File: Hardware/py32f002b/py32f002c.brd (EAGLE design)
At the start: 43.9 x 18.6 mm, 26 parts, among them IC1 PY32F002BF15P6TU, IC2 AP2114HA-3.3TRG1, J1 USB_MINI-B_SMT, Y1 DSC6083CI1A-350K000T

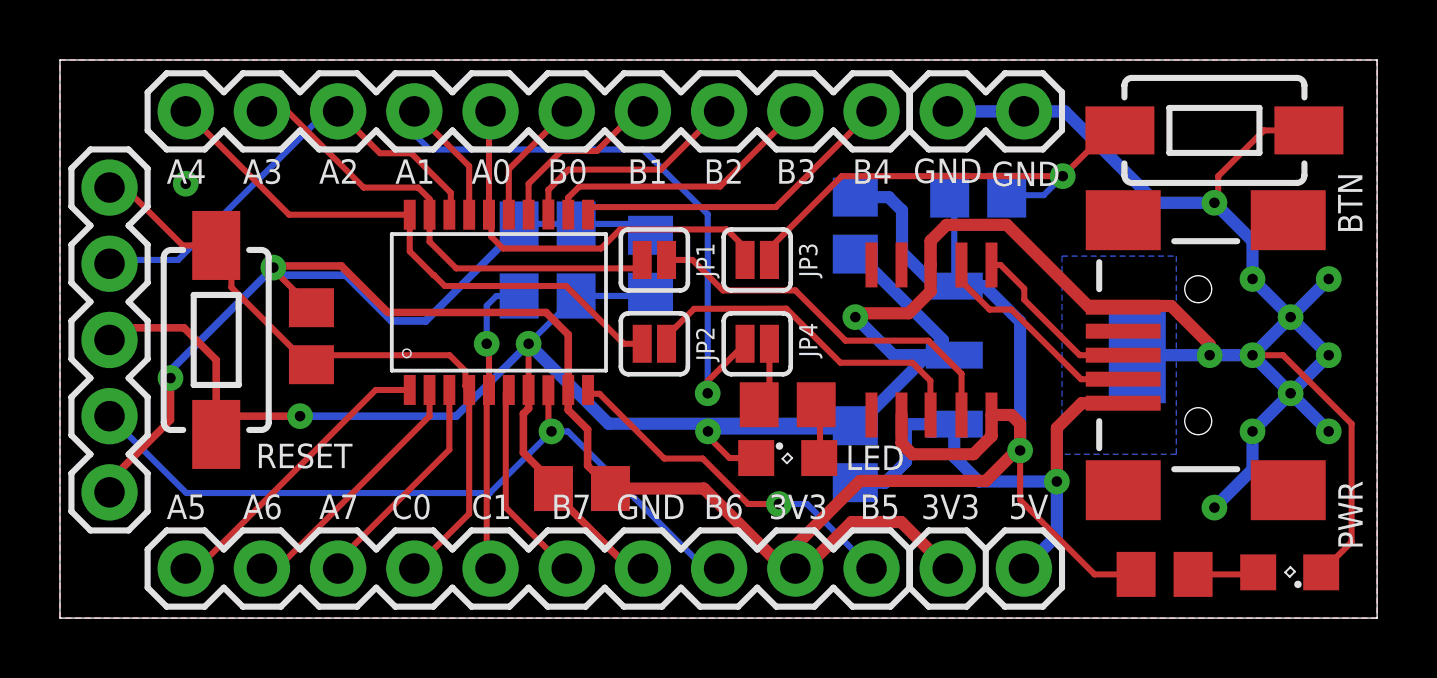
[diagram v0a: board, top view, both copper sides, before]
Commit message: Ensure button is pulled down
Ensure button is pulled down
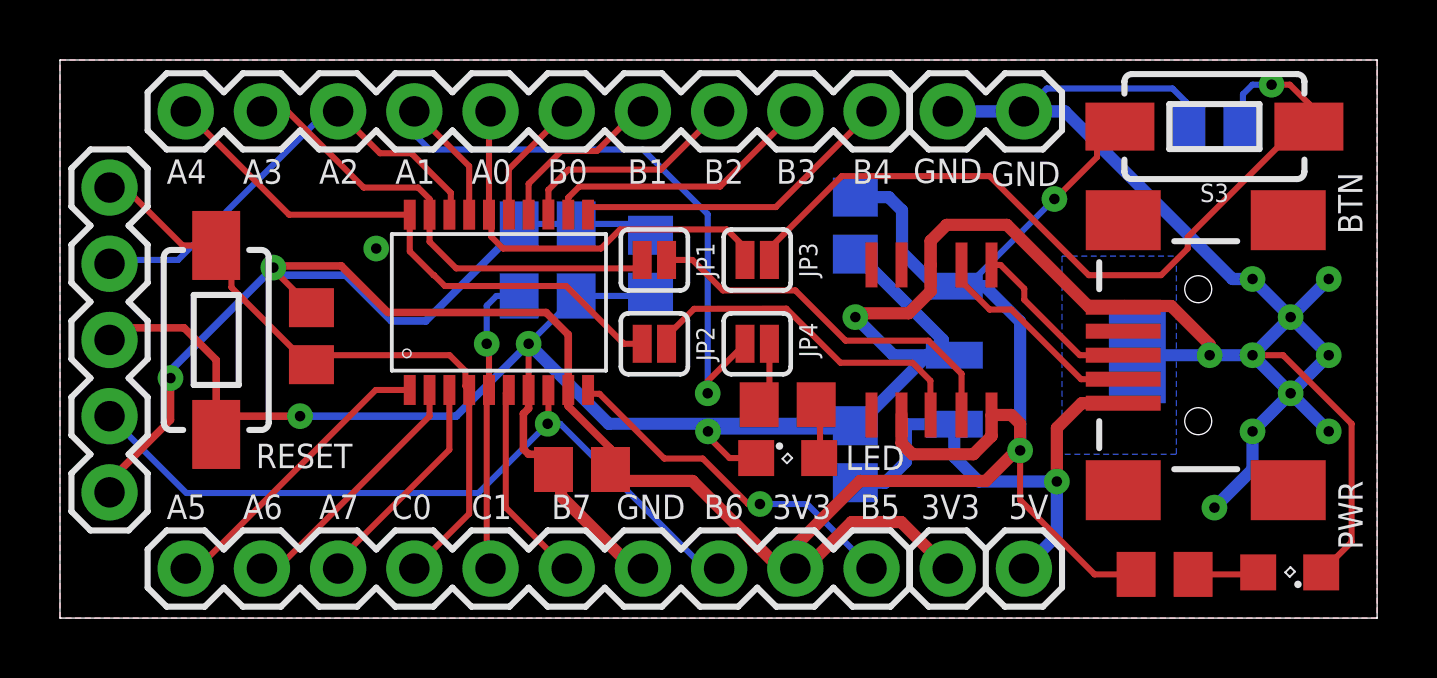
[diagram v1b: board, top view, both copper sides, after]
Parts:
- removed R2: (no value), rcl:R0805
- removed S2: RESET, SparkFun-Switches:TACTILE_SWITCH_SMD_6.0X3.5MM
- added R5: (no value), rcl:R0805
- added S3: RESET, SparkFun-Switches:TACTILE_SWITCH_SMD_6.0X3.5MM
- moved C1 0.64 mm to (17.4, 4.95)
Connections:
- net +3V3: now also S3.2; no longer R2.2
- net GND: now also R5.1; no longer S2.1
- net N$1: now also R5.2, S3.1; no longer R2.1, S2.2
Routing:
- net N$1: track 15.8 -> 27.4 mm
- net +3V3: track 95.3 -> 99.1 mm, vias 3 -> 4
- net GND: track 129.5 -> 131.0 mm, vias 16 -> 15
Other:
- board text removed: "JP1 - PA4/USB_RX JP2 - PA3/USB_TX JP3 - PA0/BTN JP4 - PA1/LED"
